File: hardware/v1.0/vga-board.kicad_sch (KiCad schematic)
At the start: 20 parts, among them J7 Conn_01x34, J9 Conn_01x06, U5 74LVC245A, U6 TLV62585

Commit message: backup
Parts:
- removed D4: GREEN, LED_SMD:LED_0402_1005Metric_Pad0.77x0.64mm_HandSolder, symbol Device:LED_Small
- removed R15: 10K, Resistor_SMD:R_0603_1608Metric, symbol Device:R_Small
- renumbered D3 to D2, J9 to J10, J7 to J9, R12 to R17, R13 to R18, R14 to R19, R16 to R20, R17 to R21, U5 to U6, U6 to U7
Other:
- moved on the sheet: D2, R19

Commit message: updated project to Kicad version 9.0
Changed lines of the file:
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@@
 (kicad_sch
-	(version 20231120)
+	(version 20250114)
 	(generator "eeschema")
-	(generator_version "8.0")
+	(generator_version "9.0")
 	(paper "A4")
+	(rectangle
+		(start 123.19 15.24)
+		(end 190.5 55.88)
+		(stroke
+			(width 0.508)
+			(type dash)
+		)
+		(fill
+			(type none)
+		)
+	)
+	(rectangle
+		(start 163.83 58.42)
+		(end 196.215 73.66)
+		(stroke
+			(width 0.508)
+			(type dash)
+		)
+		(fill
+			(type none)
+		)
+	)
+	(rectangle
+		(start 194.31 15.24)
+		(end 250.825 43.18)
+		(stroke
+			(width 0.508)
+			(type dash)
+		)
+		(fill
+			(type none)
+		)
+	)
+	(rectangle
+		(start 14.605 15.24)
+		(end 56.515 119.38)
+		(stroke
+			(width 0.508)
+			(type dash)
+		)
+		(fill
+			(type none)
+		)
+	)
+	(rectangle
+		(start 64.135 15.24)
+		(end 118.745 119.38)
+		(stroke
+			(width 0.508)
+			(type dash)
+		)
+		(fill
+			(type none)
+		)
+	)
+	(rectangle
+		(start 123.19 58.42)
+		(end 160.02 94.615)
+		(stroke
+			(width 0.508)
+			(type dash)
+		)
+		(fill
+			(type none)
+		)
+	)
+	(text "R2R DAC"
+		(exclude_from_sim no)
+		(at 65.405 20.32 0)
+		(effects
+			(font
+				(size 3.048 3.048)
+				(thickness 0.6096)
+				(bold yes)
+			)
+			(justify left bottom)
+		)
+	)
+	(text "LEDS"
+		(exclude_from_sim no)
+		(at 164.846 72.39 0)
+		(effects
+			(font
+				(size 3.048 3.048)
+				(thickness 0.6096)
+				(bold yes)
+			)
+			(justify left bottom)
+		)
+	)
+	(text "3V3 BUCK"
+		(exclude_from_sim no)
+		(at 195.58 41.91 0)
+		(effects
+			(font
+				(size 3.048 3.048)
+				(thickness 0.6096)
+				(bold yes)
+			)
+			(justify left bottom)
+		)
+	)
+	(text "RGB FPC"
+		(exclude_from_sim no)
+		(at 36.195 20.32 0)
+		(effects
+			(font
+				(size 3.048 3.048)
+				(thickness 0.6096)
+				(bold yes)
+			)
+			(justify right bottom)
+		)
+	)
+	(text "SYNC DRIVER"
+		(exclude_from_sim no)
+		(at 124.46 20.32 0)
+		(effects
+			(font
+				(size 3.048 3.048)
+				(thickness 0.6096)
+				(bold yes)
+			)
+			(justify left bottom)
+		)
+	)
+	(text "VGA CONN\n"
+		(exclude_from_sim no)
+		(at 124.46 92.71 0)
+		(effects
+			(font
+				(size 3.048 3.048)
+				(thickness 0.6096)
+				(bold yes)
+			)
+			(justify left bottom)
+		)
+	)
 	(junction
 		(at 148.59 43.18)
@@
 		)
 	)
-	(rectangle
-		(start 123.19 15.24)
-		(end 190.5 55.88)
-		(stroke
-			(width 0.508)
-			(type dash)
-		)
-		(fill
-			(type none)
-		)
-	)
-	(rectangle
-		(start 163.83 58.42)
-		(end 196.215 73.66)
-		(stroke
-			(width 0.508)
-			(type dash)
-		)
-		(fill
-			(type none)
-		)
-	)
-	(rectangle
-		(start 194.31 15.24)
-		(end 250.825 43.18)
-		(stroke
-			(width 0.508)
-			(type dash)
-		)
-		(fill
-			(type none)
-		)
-	)
-	(rectangle
-		(start 14.605 15.24)
-		(end 56.515 119.38)
-		(stroke
-			(width 0.508)
-			(type dash)
-		)
-		(fill
-			(type none)
-		)
-	)
-	(rectangle
-		(start 64.135 15.24)
-		(end 118.745 119.38)
-		(stroke
-			(width 0.508)
-			(type dash)
-		)
-		(fill
-			(type none)
-		)
-	)
-	(rectangle
-		(start 123.19 58.42)
-		(end 160.02 94.615)
-		(stroke
-			(width 0.508)
-			(type dash)
-		)
-		(fill
-			(type none)
-		)
-	)
-	(text "R2R DAC"
-		(exclude_from_sim no)
-		(at 65.405 20.32 0)
-		(effects
-			(font
-				(size 3.048 3.048)
-				(thickness 0.6096)
-				(bold yes)
-			)
-			(justify left bottom)
-		)
-	)
-	(text "LEDS"
-		(exclude_from_sim no)
-		(at 164.846 72.39 0)
-		(effects
-			(font
-				(size 3.048 3.048)
-				(thickness 0.6096)
-				(bold yes)
-			)
-			(justify left bottom)
-		)
-	)
-	(text "3V3 BUCK"
-		(exclude_from_sim no)
-		(at 195.58 41.91 0)
-		(effects
-			(font
-				(size 3.048 3.048)
-				(thickness 0.6096)
-				(bold yes)
-			)
-			(justify left bottom)
-		)
-	)
-	(text "RGB FPC"
-		(exclude_from_sim no)
-		(at 36.195 20.32 0)
-		(effects
-			(font
-				(size 3.048 3.048)
-				(thickness 0.6096)
-				(bold yes)
-			)
-			(justify right bottom)
-		)
-	)
-	(text "SYNC DRIVER"
-		(exclude_from_sim no)
-		(at 124.46 20.32 0)
-		(effects
-			(font
-				(size 3.048 3.048)
-				(thickness 0.6096)
-				(bold yes)
-			)
-			(justify left bottom)
-		)
-	)
-	(text "VGA CONN\n"
-		(exclude_from_sim no)
-		(at 124.46 92.71 0)
-		(effects
-			(font
-				(size 3.048 3.048)
-				(thickness 0.6096)
-				(bold yes)
-			)
-			(justify left bottom)
-		)
-	)
 	(label "VGA_GREEN5"
 		(at 76.835 76.2 0)
@@
 		(at 89.535 59.69)
 		(size 21.59 24.13)
+		(exclude_from_sim no)
+		(in_bom yes)
+		(on_board yes)
+		(dnp no)
 		(fields_autoplaced yes)
 		(stroke
@@
 		(at 89.535 91.44)
 		(size 21.59 24.13)
+		(exclude_from_sim no)
+		(in_bom yes)
+		(on_board yes)
+		(dnp no)
 		(fields_autoplaced yes)
 		(stroke
@@
 		(at 89.535 29.21)
 		(size 21.59 24.13)
+		(exclude_from_sim no)
+		(in_bom yes)
+		(on_board yes)
+		(dnp no)
 		(fields_autoplaced yes)
 		(stroke

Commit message: changes
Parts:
- R20, R21: footprint Resistor_SMD:R_0402_1005Metric -> Resistor_SMD:R_0603_1608Metric
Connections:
- net GND: no longer U6.4 (A2), U6.5 (A3), U6.6 (A4), U6.7 (A5), U6.8 (A6), U6.9 (A7)
- net HSYNC: now also J10.2 (Pin_2), R18.2; no longer J9.32 (Pin_32), U6.3 (A1)
- net VGA_HSYNC: now also J9.32 (Pin_32), U6.3 (A1); no longer J10.2 (Pin_2), R18.2
- net VGA_VSYNC: now also J9.30 (Pin_30), U6.2 (A0); no longer J10.1 (Pin_1), R17.2
- net VSYNC: now also J10.1 (Pin_1), R17.2; no longer J9.30 (Pin_30), U6.2 (A0)
- no-connect marks 3 -> 15

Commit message: backup
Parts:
- removed C23, C24: 10uf, Capacitor_SMD:C_0805_2012Metric, symbol Device:C_Small
- removed C29: 22uf, Capacitor_SMD:C_0805_2012Metric, symbol Device:C_Small
- C27: value 22uf -> 4.7uf
- C28: value 22uf -> 10uf
- L2: value 1uh -> 2.2uh
- R19: value 1K -> 1k
- R20: value 450K -> 450k
- R21: value 100K -> 100k
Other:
- moved on the sheet: C27, C28, L2, R20, R21, U7

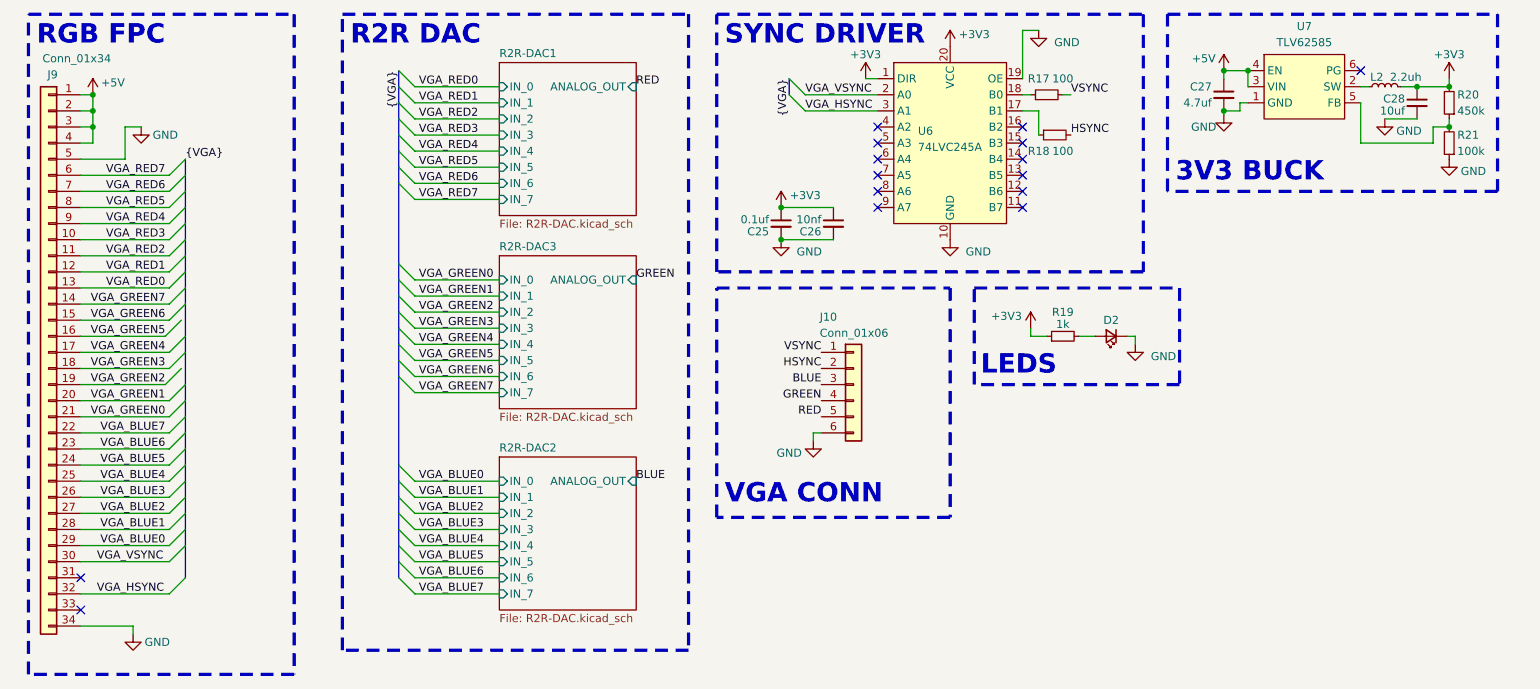
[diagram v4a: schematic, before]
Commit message: added pmod connectors instead of leds
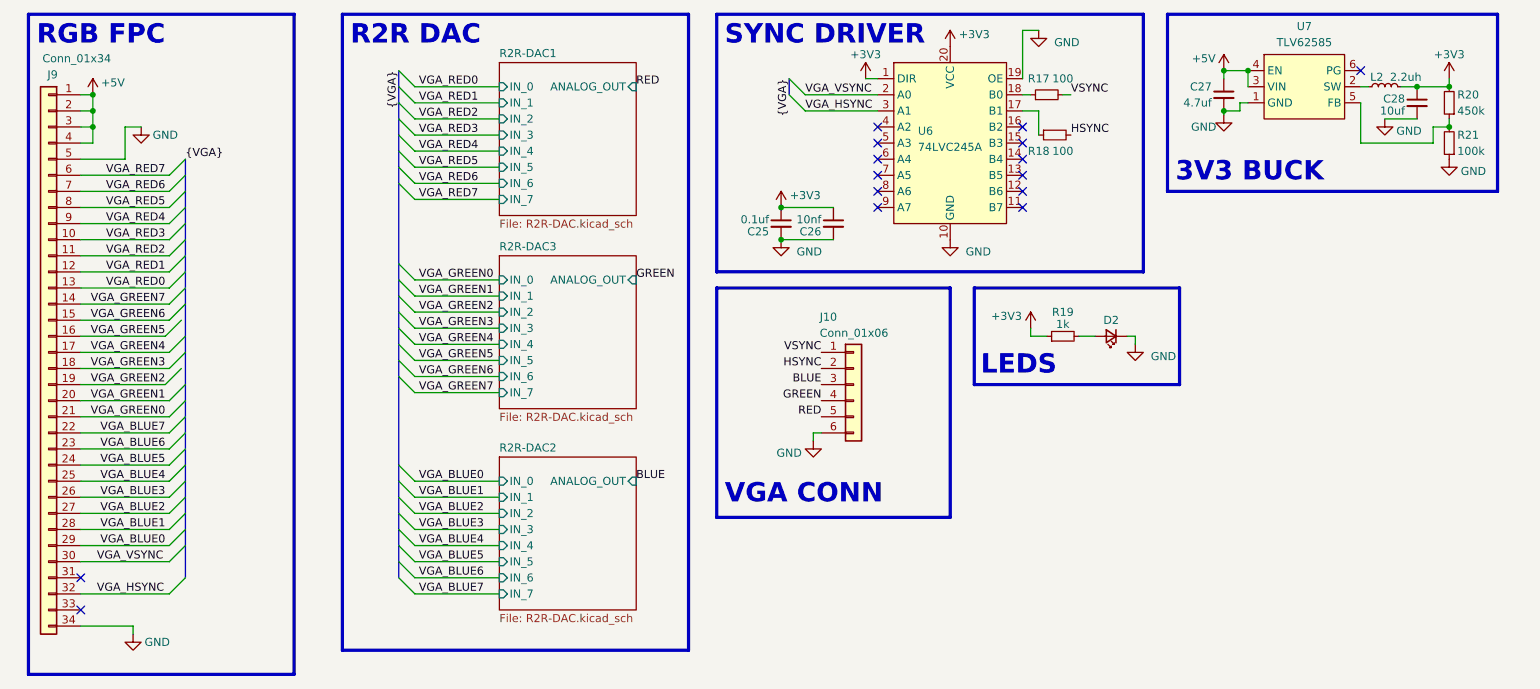
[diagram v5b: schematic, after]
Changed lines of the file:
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@@
 		(stroke
 			(width 0.508)
-			(type dash)
+			(type solid)
 		)
 		(fill
@@
 		(stroke
 			(width 0.508)
-			(type dash)
+			(type solid)
 		)
 		(fill
@@
 		(stroke
 			(width 0.508)
-			(type dash)
+			(type solid)
 		)
 		(fill
@@
 		(stroke
 			(width 0.508)
-			(type dash)
+			(type solid)
 		)
 		(fill
@@
 		(stroke
 			(width 0.508)
-			(type dash)
+			(type solid)
 		)
 		(fill
@@
 		(stroke
 			(width 0.508)
-			(type dash)
+			(type solid)
 		)
 		(fill

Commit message: first schematic iteration done
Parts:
- R19: value 1k -> 4.7k
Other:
- note added: "LED"
- note removed: "LEDS"
- moved on the sheet: D2, R19
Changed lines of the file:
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@@
 	(rectangle
 		(start 163.83 58.42)
-		(end 196.215 73.66)
+		(end 190.5 73.66)
 		(stroke
 			(width 0.508)
@@
 		)
 	)
-	(text "LEDS"
+	(text "LED"
 		(exclude_from_sim no)
 		(at 164.846 72.39 0)
@@
 	(wire
 		(pts
-			(xy 189.23 67.31) (xy 189.23 66.04)
+			(xy 187.96 67.31) (xy 187.96 64.77)
 		)
 		(stroke
@@
 	(wire
 		(pts
-			(xy 172.72 66.04) (xy 172.72 64.77)
+			(xy 171.45 64.77) (xy 171.45 63.5)
 		)
 		(stroke
@@
 	(wire
 		(pts
-			(xy 189.23 66.04) (xy 187.96 66.04)
+			(xy 187.96 64.77) (xy 186.69 64.77)
 		)
 		(stroke
@@
 	(wire
 		(pts
-			(xy 180.34 66.04) (xy 182.88 66.04)
+			(xy 179.07 64.77) (xy 181.61 64.77)
 		)
 		(stroke
@@
 	(wire
 		(pts
-			(xy 175.26 66.04) (xy 172.72 66.04)
+			(xy 173.99 64.77) (xy 171.45 64.77)
 		)
 		(stroke
@@
 	(symbol
 		(lib_id "power:+3V3")
-		(at 172.72 64.77 0)
+		(at 171.45 63.5 0)
 		(mirror y)
 		(unit 1)
@@
 		(dnp no)
 		(property "Reference" "#PWR59"
-			(at 172.72 68.58 0)
+			(at 171.45 67.31 0)
 			(effects
 				(font
@@
 		)
 		(property "Value" "+3V3"
-			(at 168.91 62.865 0)
+			(at 167.64 61.595 0)
 			(effects
 				(font
@@
 		)
 		(property "Footprint" ""
-			(at 172.72 64.77 0)
+			(at 171.45 63.5 0)
 			(effects
 				(font
@@
 		)
 		(property "Datasheet" ""
-			(at 172.72 64.77 0)
+			(at 171.45 63.5 0)
 			(effects
 				(font
@@
 		)
 		(property "Description" "Power symbol creates a global label with name \"+3V3\""
-			(at 172.72 64.77 0)
+			(at 171.45 63.5 0)
 			(effects
 				(font
@@
 	(symbol
 		(lib_id "power:GND")
-		(at 189.23 67.31 0)
+		(at 187.96 67.31 0)
+		(mirror y)
 		(unit 1)
 		(exclude_from_sim no)
@@
 		(dnp no)
 		(property "Reference" "#PWR61"
-			(at 189.23 73.66 0)
+			(at 187.96 73.66 0)
 			(effects
 				(font
@@
 		)
 		(property "Value" "GND"
-			(at 193.675 69.215 0)
+			(at 184.404 69.342 0)
 			(effects
 				(font
@@
 		)
 		(property "Footprint" ""
-			(at 189.23 67.31 0)
+			(at 187.96 67.31 0)
 			(effects
 				(font
@@
 		)
 		(property "Datasheet" ""
-			(at 189.23 67.31 0)
+			(at 187.96 67.31 0)
 			(effects
 				(font
@@
 		)
 		(property "Description" "Power symbol creates a global label with name \"GND\" , ground"
-			(at 189.23 67.31 0)
+			(at 187.96 67.31 0)
 			(effects
 				(font
@@
 	(symbol
 		(lib_id "Device:LED_Small")
-		(at 185.42 66.04 180)
+		(at 184.15 64.77 180)
 		(unit 1)
 		(exclude_from_sim no)
@@
 		(dnp no)
 		(property "Reference" "D2"
-			(at 185.42 63.5 0)
+			(at 184.15 62.23 0)
 			(effects
 				(font
@@
 		)
 		(property "Value" "GREEN"
-			(at 185.3565 62.865 0)
+			(at 184.0865 61.595 0)
 			(effects
 				(font
@@
 		)
 		(property "Footprint" "LED_SMD:LED_0402_1005Metric_Pad0.77x0.64mm_HandSolder"
-			(at 185.42 66.04 90)
+			(at 184.15 64.77 90)
 			(effects
 				(font
@@
 		)
 		(property "Datasheet" "~"
-			(at 185.42 66.04 90)
+			(at 184.15 64.77 90)
 			(effects
 				(font
@@
 		)
 		(property "Description" "Light emitting diode, small symbol"
-			(at 185.42 66.04 0)
+			(at 184.15 64.77 0)
+			(effects
+				(font
+					(size 1.27 1.27)
+				)
+				(hide yes)
+			)
+		)
+		(property "Sim.Pin" "1=K 2=A"
+			(at 184.15 64.77 0)
 			(effects
 				(font
@@
 	(symbol
 		(lib_id "Device:R_Small")
-		(at 177.8 66.04 90)
+		(at 176.53 64.77 90)
 		(unit 1)
 		(exclude_from_sim no)
@@
 		(dnp no)
 		(property "Reference" "R19"
-			(at 177.8 62.23 90)
+			(at 176.53 60.96 90)
 			(effects
 				(font
@@
 			)
 		)
-		(property "Value" "1k"
-			(at 177.8 64.135 90)
+		(property "Value" "4.7k"
+			(at 176.53 62.865 90)
 			(effects
 				(font
@@
 		)
 		(property "Footprint" "Resistor_SMD:R_0603_1608Metric"
-			(at 177.8 66.04 0)
+			(at 176.53 64.77 0)
 			(effects
 				(font
@@
 		)
 		(property "Datasheet" "~"
-			(at 177.8 66.04 0)
+			(at 176.53 64.77 0)
 			(effects
 				(font
@@
 		)
 		(property "Description" "Resistor, small symbol"
-			(at 177.8 66.04 0)
+			(at 176.53 64.77 0)
 			(effects
 				(font

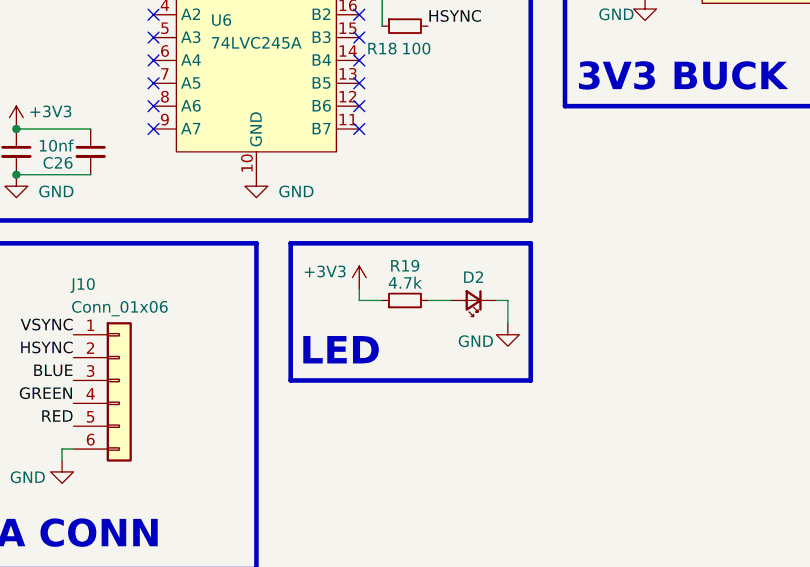
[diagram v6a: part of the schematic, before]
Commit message: did PORT0 routing
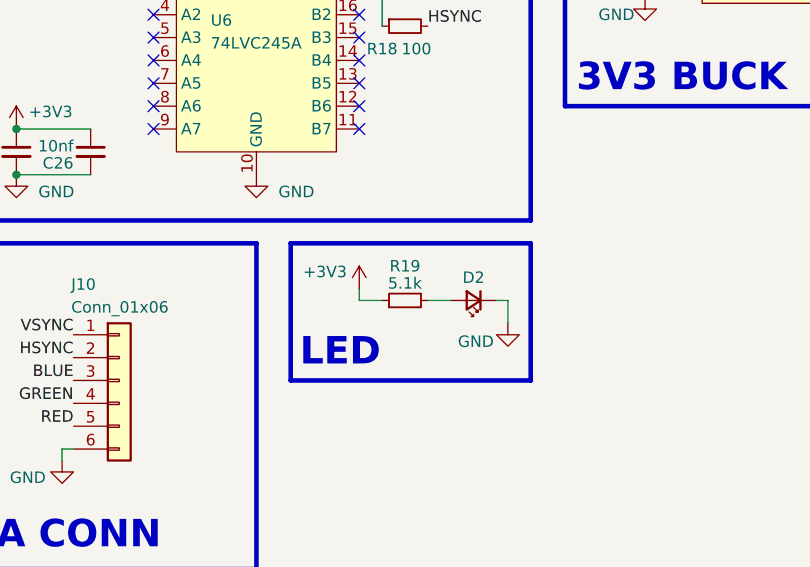
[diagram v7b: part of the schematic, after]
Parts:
- D2: value GREEN -> ~
- R19: value 4.7k -> 5.1k
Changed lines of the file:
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@@
 			)
 		)
-		(property "Value" "GREEN"
+		(property "Value" "~"
 			(at 184.0865 61.595 0)
 			(effects
@@
 			)
 		)
-		(property "Value" "4.7k"
+		(property "Value" "5.1k"
 			(at 176.53 62.865 90)
 			(effects
